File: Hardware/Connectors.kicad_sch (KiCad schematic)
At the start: 22 parts, among them J1 Conn_01x03, J2 Conn_01x07, SW6 SW_Push, SW7 SW_Push

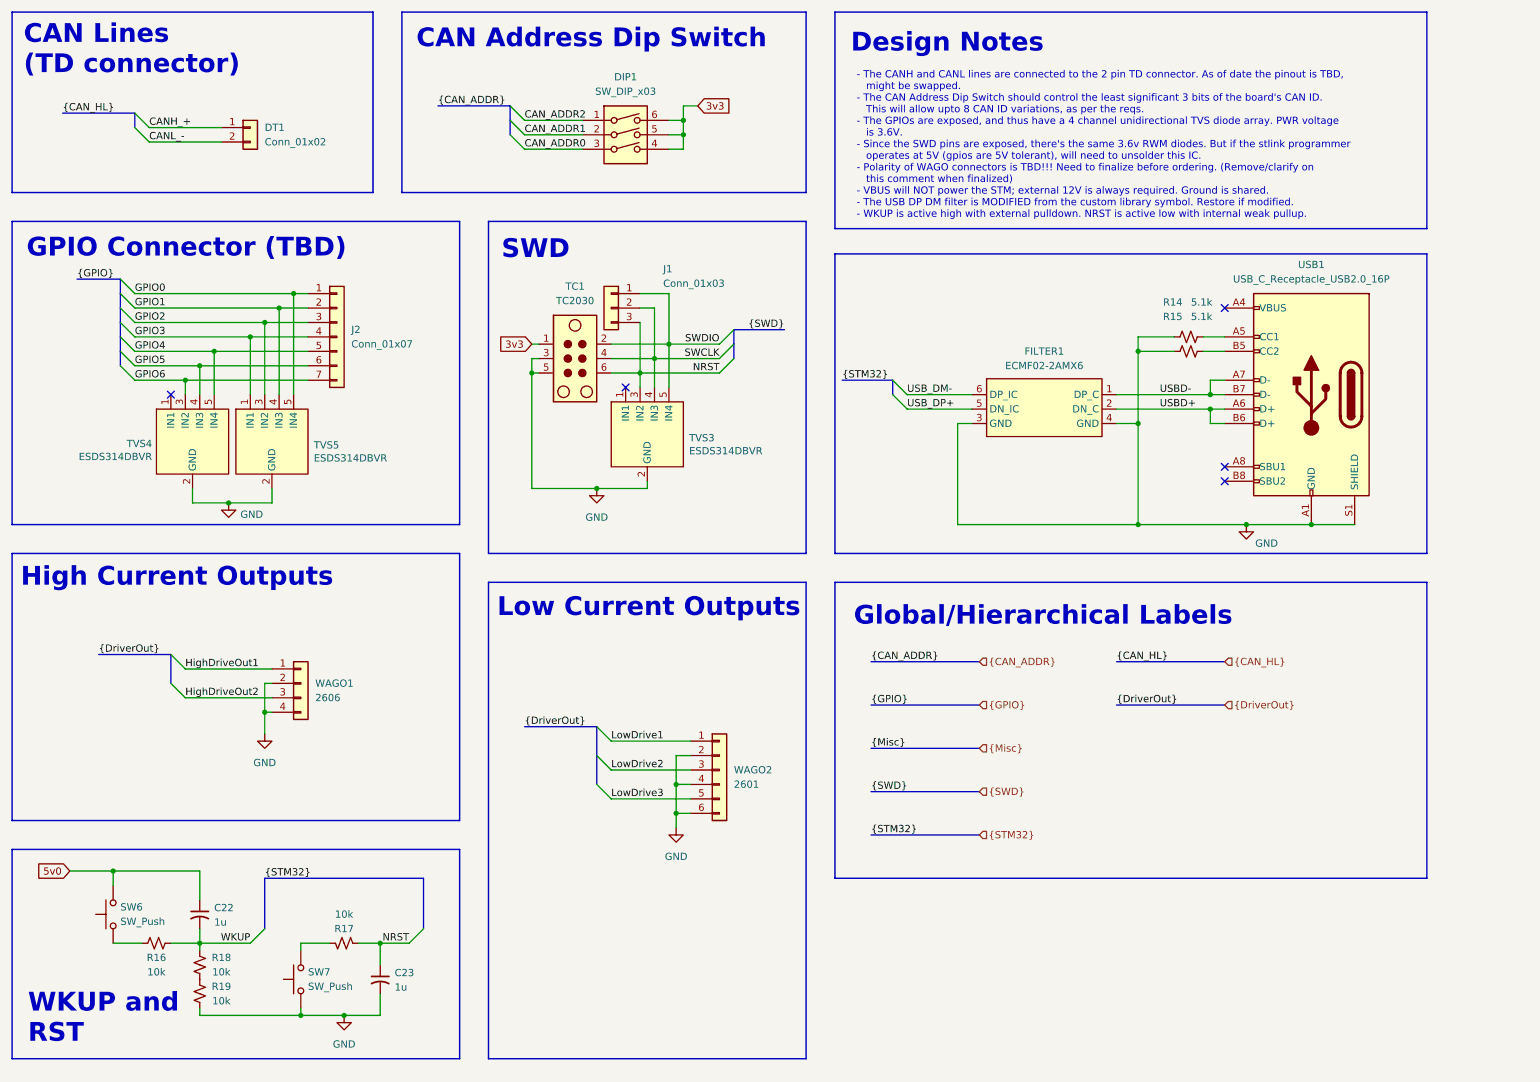
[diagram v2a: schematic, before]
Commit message: Replaced G0B1KET6 with KET6N in schematic
- Updated the schematic with new symbol and pinout.
- Updated the rest of the schematic with all resulting changes
	- This includes the 8 output channels, 7 GPIOs, and slightly
	  different WAGO connector configuration.
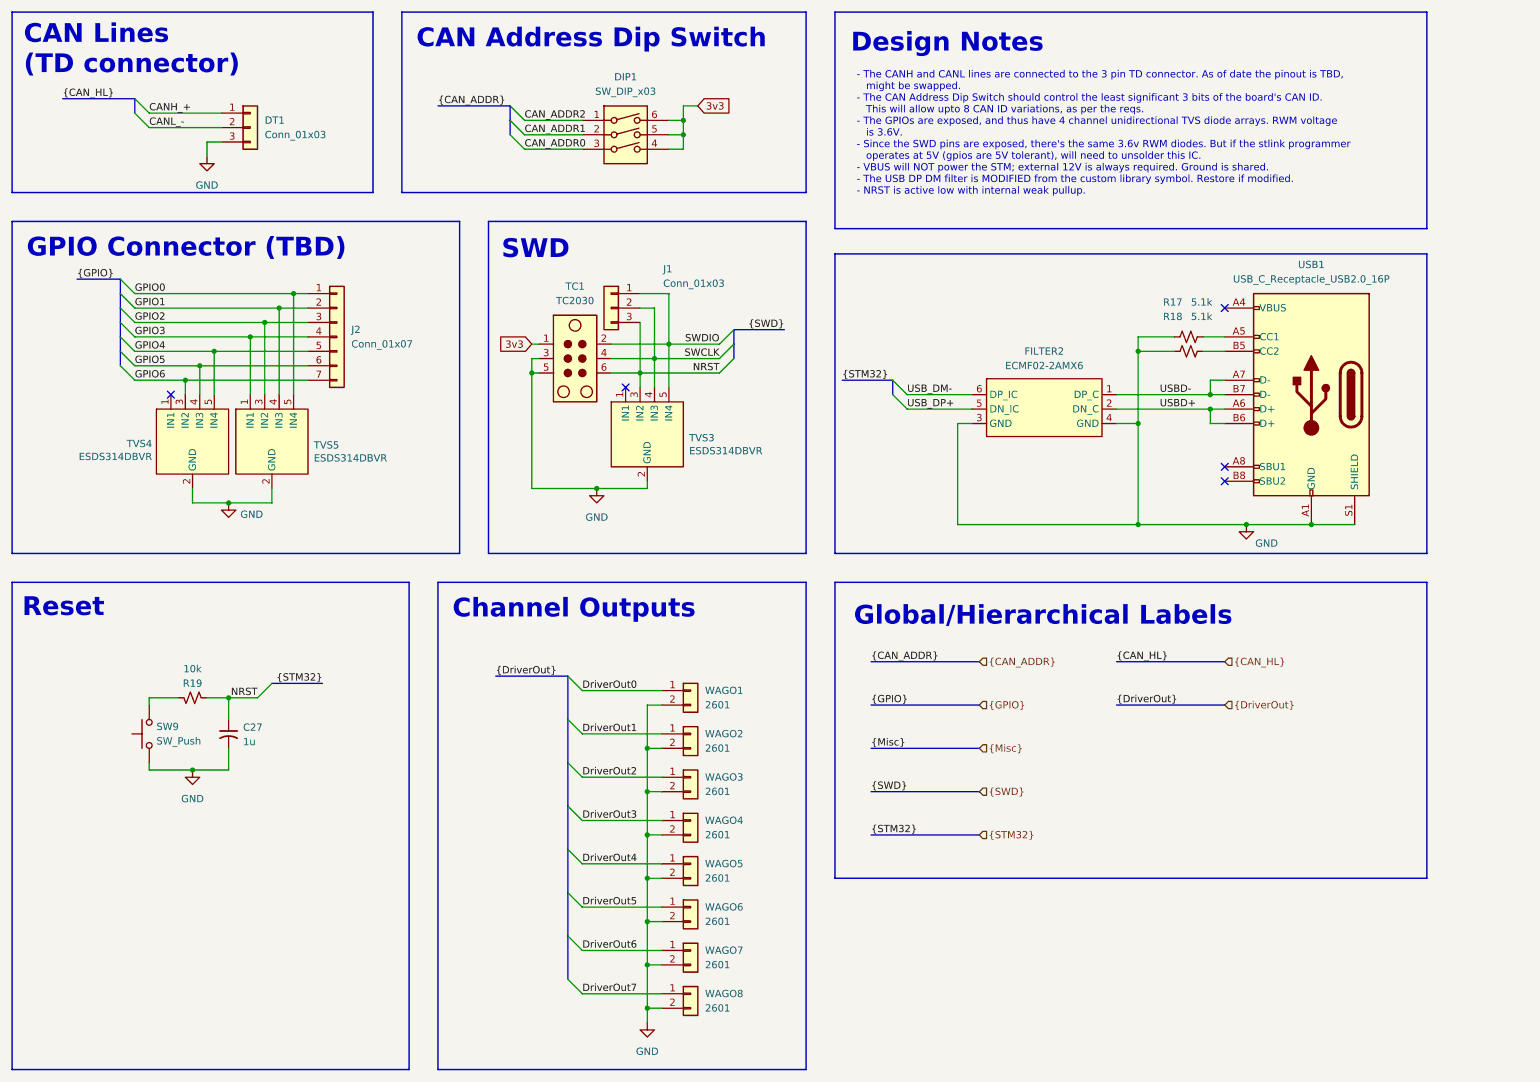
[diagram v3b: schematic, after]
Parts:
- removed C22: 1u, Capacitor_SMD:C_0603_1608Metric_Pad1.08x0.95mm_HandSolder, symbol Device:C_Small_US
- removed DT1: Conn_01x02, TerminalBlock:TerminalBlock_MaiXu_MX126-5.0-02P_1x02_P5.00mm, symbol Connector_Generic:Conn_01x02
- removed R16, R18, R19: 10k, Resistor_SMD:R_0603_1608Metric_Pad0.98x0.95mm_HandSolder, symbol Device:R_Small_US
- removed SW6: SW_Push, Button_Switch_SMD:SW_Push_1P1T_NO_CK_KSC7xxJ, symbol Switch:SW_Push
- removed WAGO1: 2606, symbol Connector_Generic:Conn_01x04
- removed WAGO2: 2601, TerminalBlock_WAGO:TerminalBlock_WAGO_2601-1106_1x06_P3.50mm_Horizontal, symbol Connector_Generic:Conn_01x06
- added DT1: Conn_01x03, symbol Connector_Generic:Conn_01x03
- added WAGO1, WAGO2, WAGO3, WAGO4, WAGO5, WAGO6, WAGO7, WAGO8: 2601, symbol Connector_Generic:Conn_01x02
- renumbered C23 to C27, FILTER1 to FILTER2, R14 to R17, R15 to R18, R17 to R19, SW7 to SW9
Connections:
- net CANH_+: now also DT1.1 (Pin_1)
- net CANL_-: now also DT1.2 (Pin_2)
- net GND: now also DT1.3 (Pin_3), WAGO1.2 (Pin_2), WAGO2.2 (Pin_2), WAGO3.2 (Pin_2), WAGO4.2 (Pin_2), WAGO5.2 (Pin_2), WAGO6.2 (Pin_2), WAGO7.2 (Pin_2), WAGO8.2 (Pin_2)
- new net DriverOut0: WAGO1.1 (Pin_1)
- new net DriverOut1: WAGO2.1 (Pin_1)
- new net DriverOut2: WAGO3.1 (Pin_1)
- new net DriverOut3: WAGO4.1 (Pin_1)
- new net DriverOut4: WAGO5.1 (Pin_1)
- new net DriverOut5: WAGO6.1 (Pin_1)
- new net DriverOut6: WAGO7.1 (Pin_1)
- new net DriverOut7: WAGO8.1 (Pin_1)
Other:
- note added: "- The CANH and CANL lines are connected to the 3 pin TD connector. As of date the pinout is TBD, might be swapped. - The CAN Address Dip Switch should control the least significant 3 bits of the board's CAN ID. This will allow upto 8 CAN ID variations, as per the reqs. - The GPIOs are exposed, and thus have 4 channel unidirectional TVS diode arrays. RWM voltage is 3.6V. - Since the SWD pins are e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"
- note added: "Channel Outputs"
- note added: "Reset"
- note removed: "- The CANH and CANL lines are connected to the 2 pin TD connector. As of date the pinout is TBD, might be swapped. - The CAN Address Dip Switch should control the least significant 3 bits of the board's CAN ID. This will allow upto 8 CAN ID variations, as per the reqs. - The GPIOs are exposed, and thus have a 4 channel unidirectional TVS diode array. PWR voltage is 3.6V. - Since the SWD pins are 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"
- note removed: "High Current Outputs"
- note removed: "Low Current Outputs"
- note removed: "WKUP and RST"
- moved on the sheet: C27, R19, SW9

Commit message: Finished the board
- Board layout and routing is finished. Need to fix ~30 ERC errors and
  add thorough notes throughout, but otherwise that's it.
- Once ERC errors are resolved, will post BOM and Gerbers as a release.
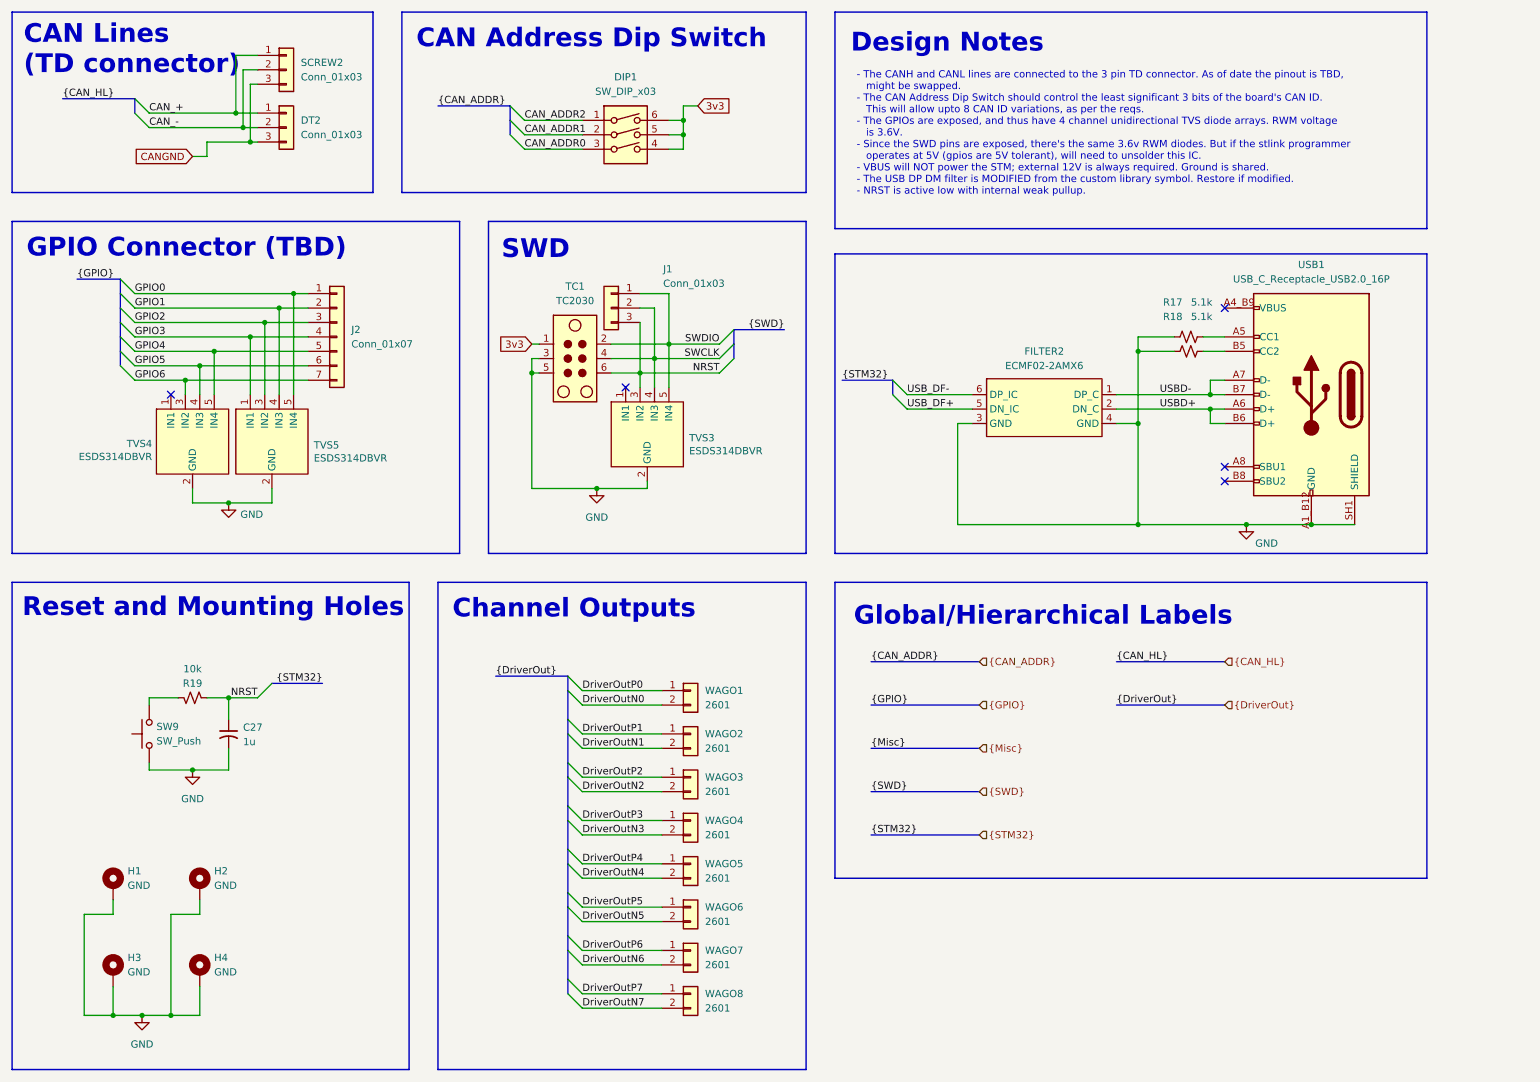
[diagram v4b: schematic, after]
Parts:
- added H1, H2, H3, H4: GND, MountingHole:MountingHole_3.5mm_Pad_Via, symbol Mechanical:MountingHole_Pad
- added SCREW2: Conn_01x03, TerminalBlock:TerminalBlock_MaiXu_MX126-5.0-03P_1x03_P5.00mm, symbol Connector_Generic:Conn_01x03
- DT2: renamed from DT1; footprint (none) -> footprints:TE_DTF13-3P
- FILTER2: footprint (none) -> footprints:ECMF02-2AMX6_QFN-6L
- USB1: footprint (none) -> footprints:SHOUHAN_TYPE-C_16PIN_2MD__073_
- WAGO1, WAGO2, WAGO3, WAGO4, WAGO5, WAGO6, WAGO7, WAGO8: footprint (none) -> TerminalBlock_WAGO:TerminalBlock_WAGO_2601-1102_1x02_P3.50mm_Horizontal
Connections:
- net GND: now also USB1.A1_B12 (GND), USB1.B1_A12 (GND), USB1.SH1 (SHIELD), USB1.SH2 (SHIELD), USB1.SH3 (SHIELD), USB1.SH4 (SHIELD), H1.1, H2.1, H3.1, H4.1; no longer DT2.3 (Pin_3), USB1.A1 (GND), USB1.A12 (GND), USB1.B1 (GND), USB1.B12 (GND), USB1.S1 (SHIELD), WAGO1.2 (Pin_2), WAGO2.2 (Pin_2), WAGO3.2 (Pin_2), WAGO4.2 (Pin_2), WAGO5.2 (Pin_2), WAGO6.2 (Pin_2), WAGO7.2 (Pin_2), WAGO8.2 (Pin_2)
- net CANH_+ renamed CAN_+
- net CAN_+: now also SCREW2.1 (Pin_1)
- net CANL_- renamed CAN_-
- net CAN_-: now also SCREW2.2 (Pin_2)
- net DriverOut0 renamed DriverOutP0
- net DriverOut1 renamed DriverOutP1
- net DriverOut2 renamed DriverOutP2
- net DriverOut3 renamed DriverOutP3
- net DriverOut4 renamed DriverOutP4
- net DriverOut5 renamed DriverOutP5
- net DriverOut6 renamed DriverOutP6
- net DriverOut7 renamed DriverOutP7
- net USB_DM- renamed USB_DF-
- net USB_DP+ renamed USB_DF+
- new net: USB1.A4_B9 (VBUS), USB1.B4_A9 (VBUS)
- new net CANGND: DT2.3 (Pin_3), SCREW2.3 (Pin_3)
- new net DriverOutN0: WAGO1.2 (Pin_2)
- new net DriverOutN1: WAGO2.2 (Pin_2)
- new net DriverOutN2: WAGO3.2 (Pin_2)
- new net DriverOutN3: WAGO4.2 (Pin_2)
- new net DriverOutN4: WAGO5.2 (Pin_2)
- new net DriverOutN5: WAGO6.2 (Pin_2)
- new net DriverOutN6: WAGO7.2 (Pin_2)
- new net DriverOutN7: WAGO8.2 (Pin_2)
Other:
- note added: "Reset and Mounting Holes"
- note removed: "Reset"
- moved on the sheet: DT2, USB1
